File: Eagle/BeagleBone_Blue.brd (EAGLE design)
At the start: 86.4 x 54.6 mm, 297 parts, among them M1 JST_ZH_2, M2 JST_ZH_2, M3 JST_ZH_2, M4 JST_ZH_2, P10 SCHA5B0200, Q3 MOSFET-N, U1 TPD4S012_DRY_6, U4 TPD4S012_DRY_6, U5 24LC_32AT-I/OT, U6 SN74LVC1G07_DCK_5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

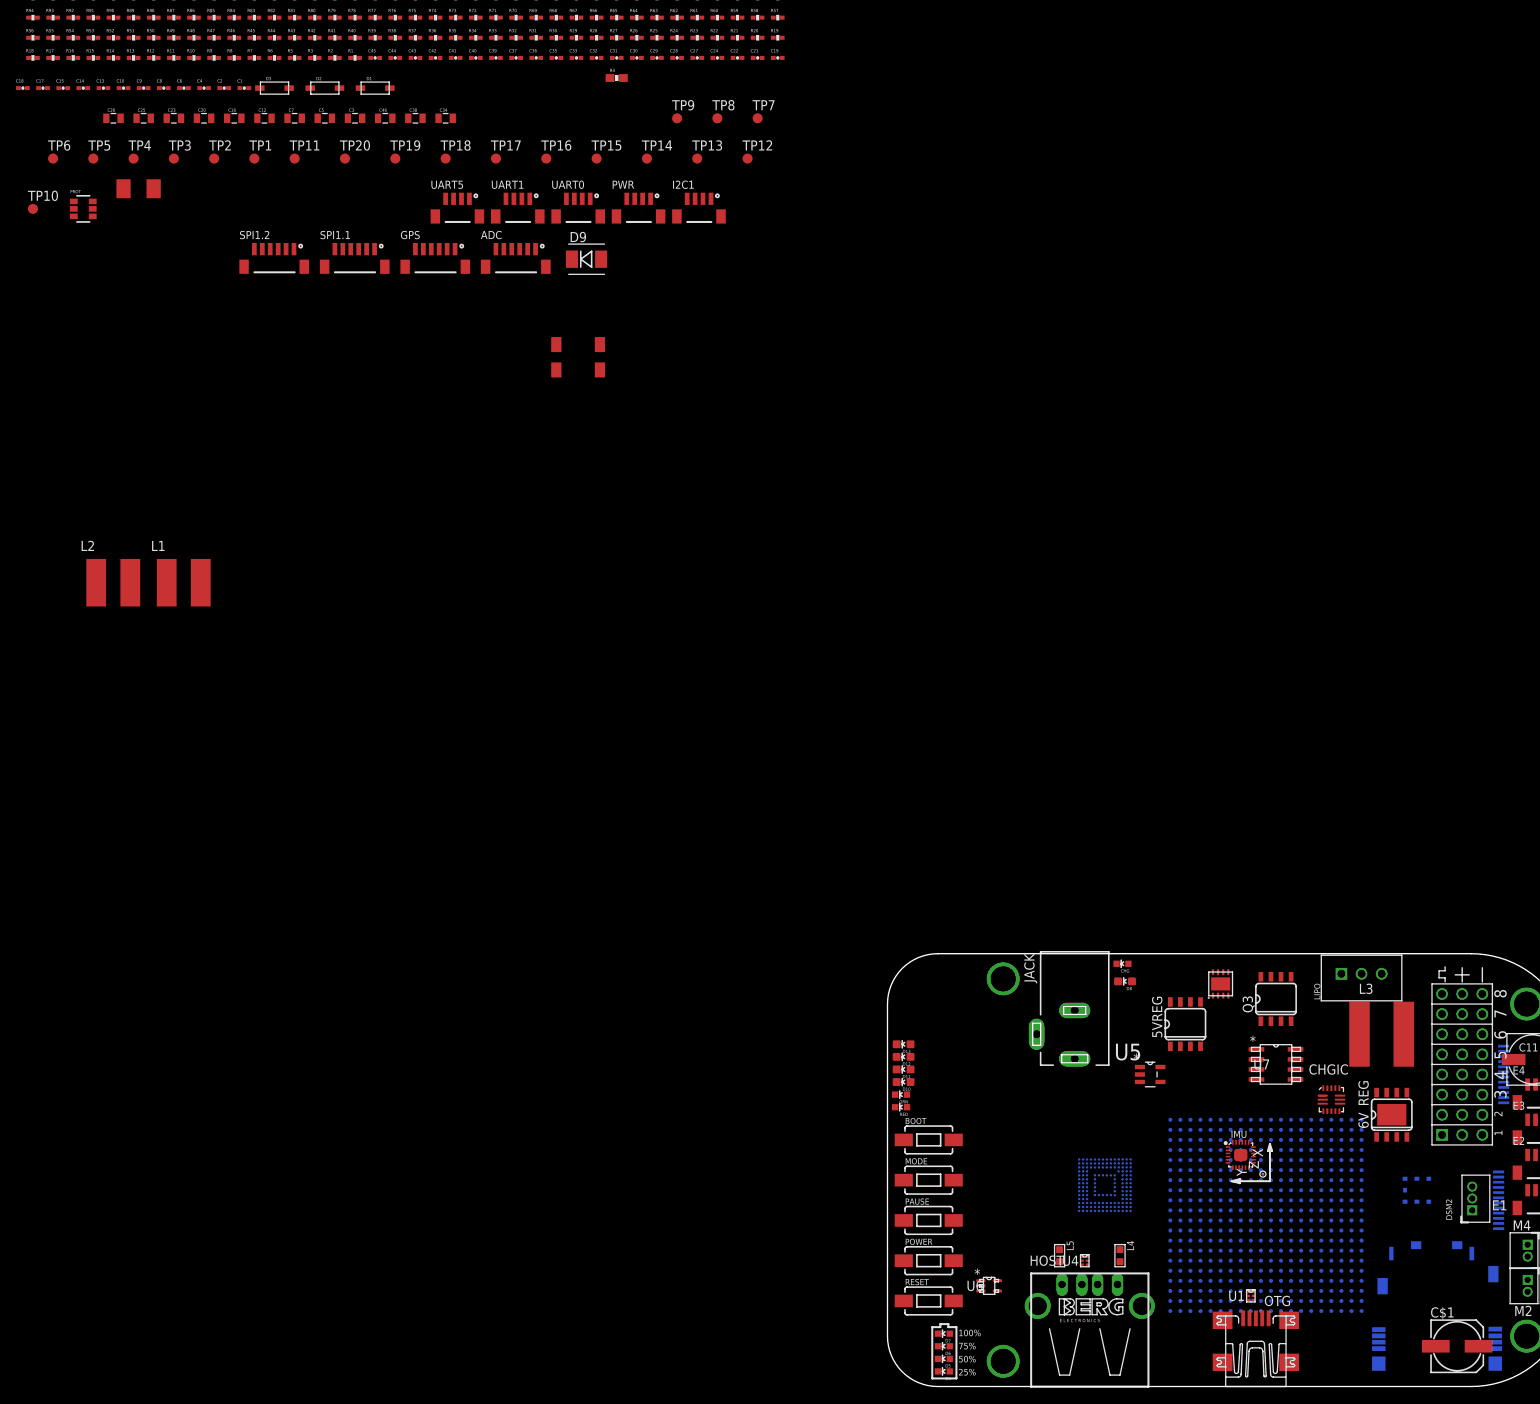
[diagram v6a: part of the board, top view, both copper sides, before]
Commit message: Rough placed a bunch of parts
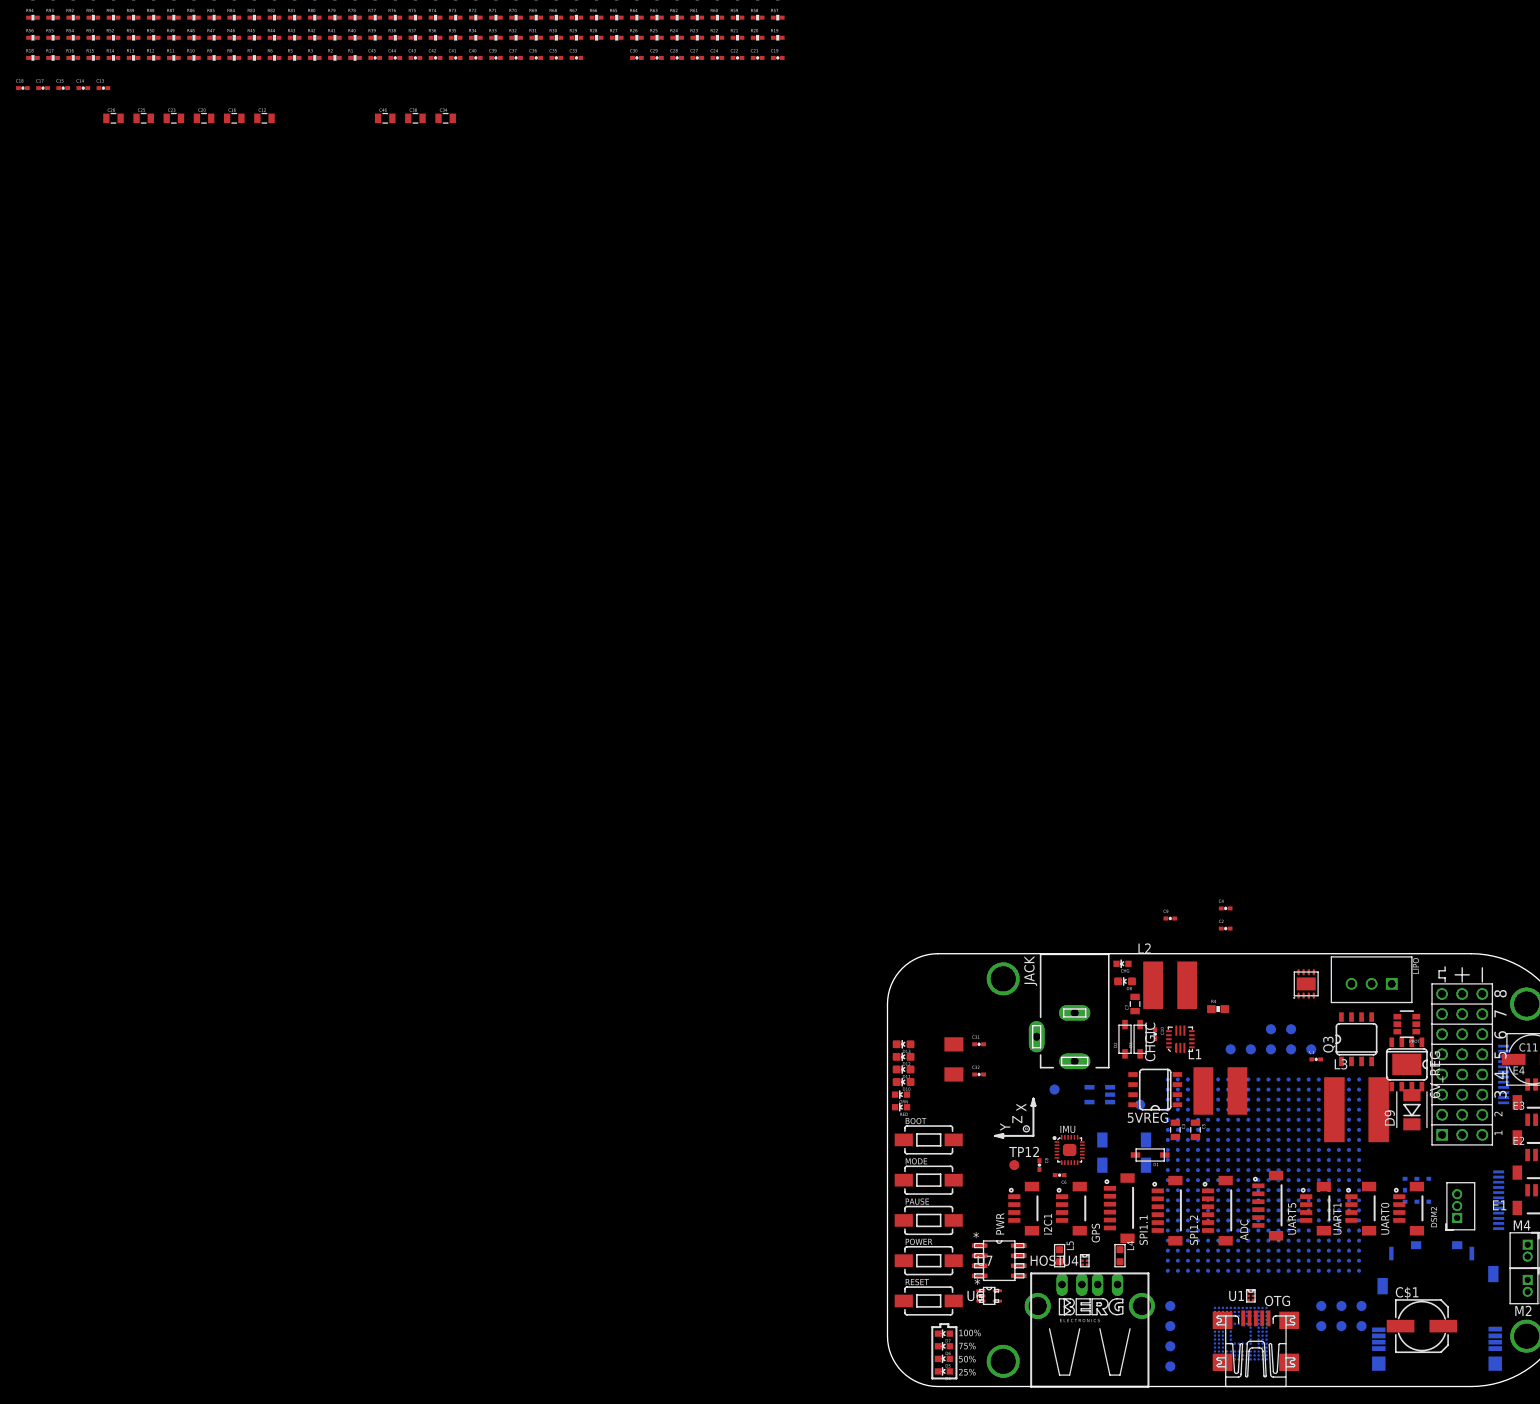
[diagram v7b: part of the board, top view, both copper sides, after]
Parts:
- moved TP6 215.8 mm to (54.6, -44.5), flipped to the bottom
- moved TP4 212.0 mm to (57.1, -47.0), flipped to the bottom
- moved TP3 210.1 mm to (59.7, -47.0), flipped to the bottom
- moved TP2 203.0 mm to (57.1, -44.5), flipped to the bottom
- moved TP10 203.0 mm to (35.6, -49.5), flipped to the bottom
- moved TP1 201.2 mm to (59.7, -44.5), flipped to the bottom
- moved PROT 196.1 mm to (65.4, -8.89), turned to 180 degrees
- moved TP11 188.2 mm to (35.6, -52.1), flipped to the bottom
- moved C1 182.5 mm to (54.0, -13.3)
- moved TP5 178.0 mm to (31.8, -19.1), flipped to the bottom
- moved C10 176.6 mm to (33.7, -10.2), turned to 270 degrees
- moved C6 176.1 mm to (21.6, -27.9), turned to 180 degrees
- moved C8 175.1 mm to (19.1, -26.7), turned to 270 degrees
- moved SPI1.2 172.7 mm to (40.3, -34.9), turned to 90 degrees
- moved C5 168.4 mm to (38.7, -22.2), turned to 270 degrees
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
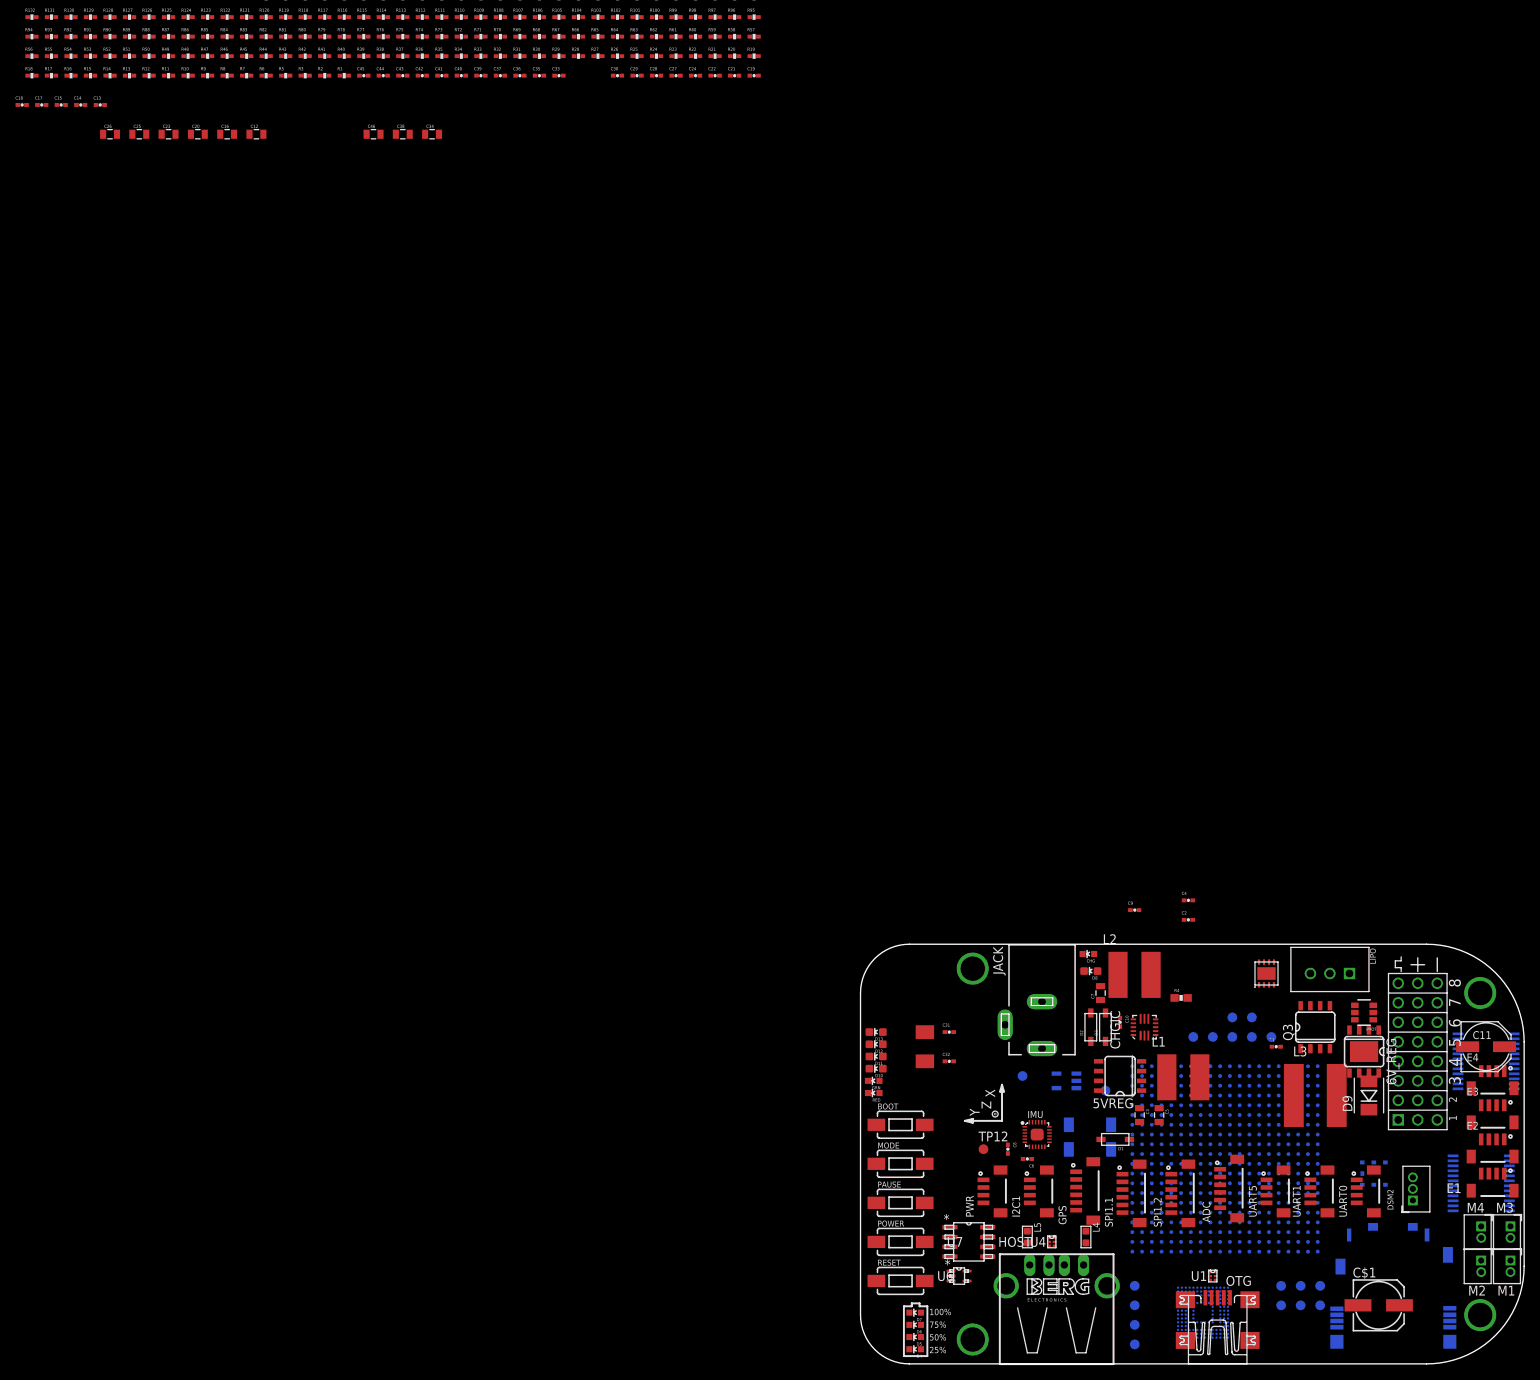
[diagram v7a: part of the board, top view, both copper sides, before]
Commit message: Rough placed a bunch of parts
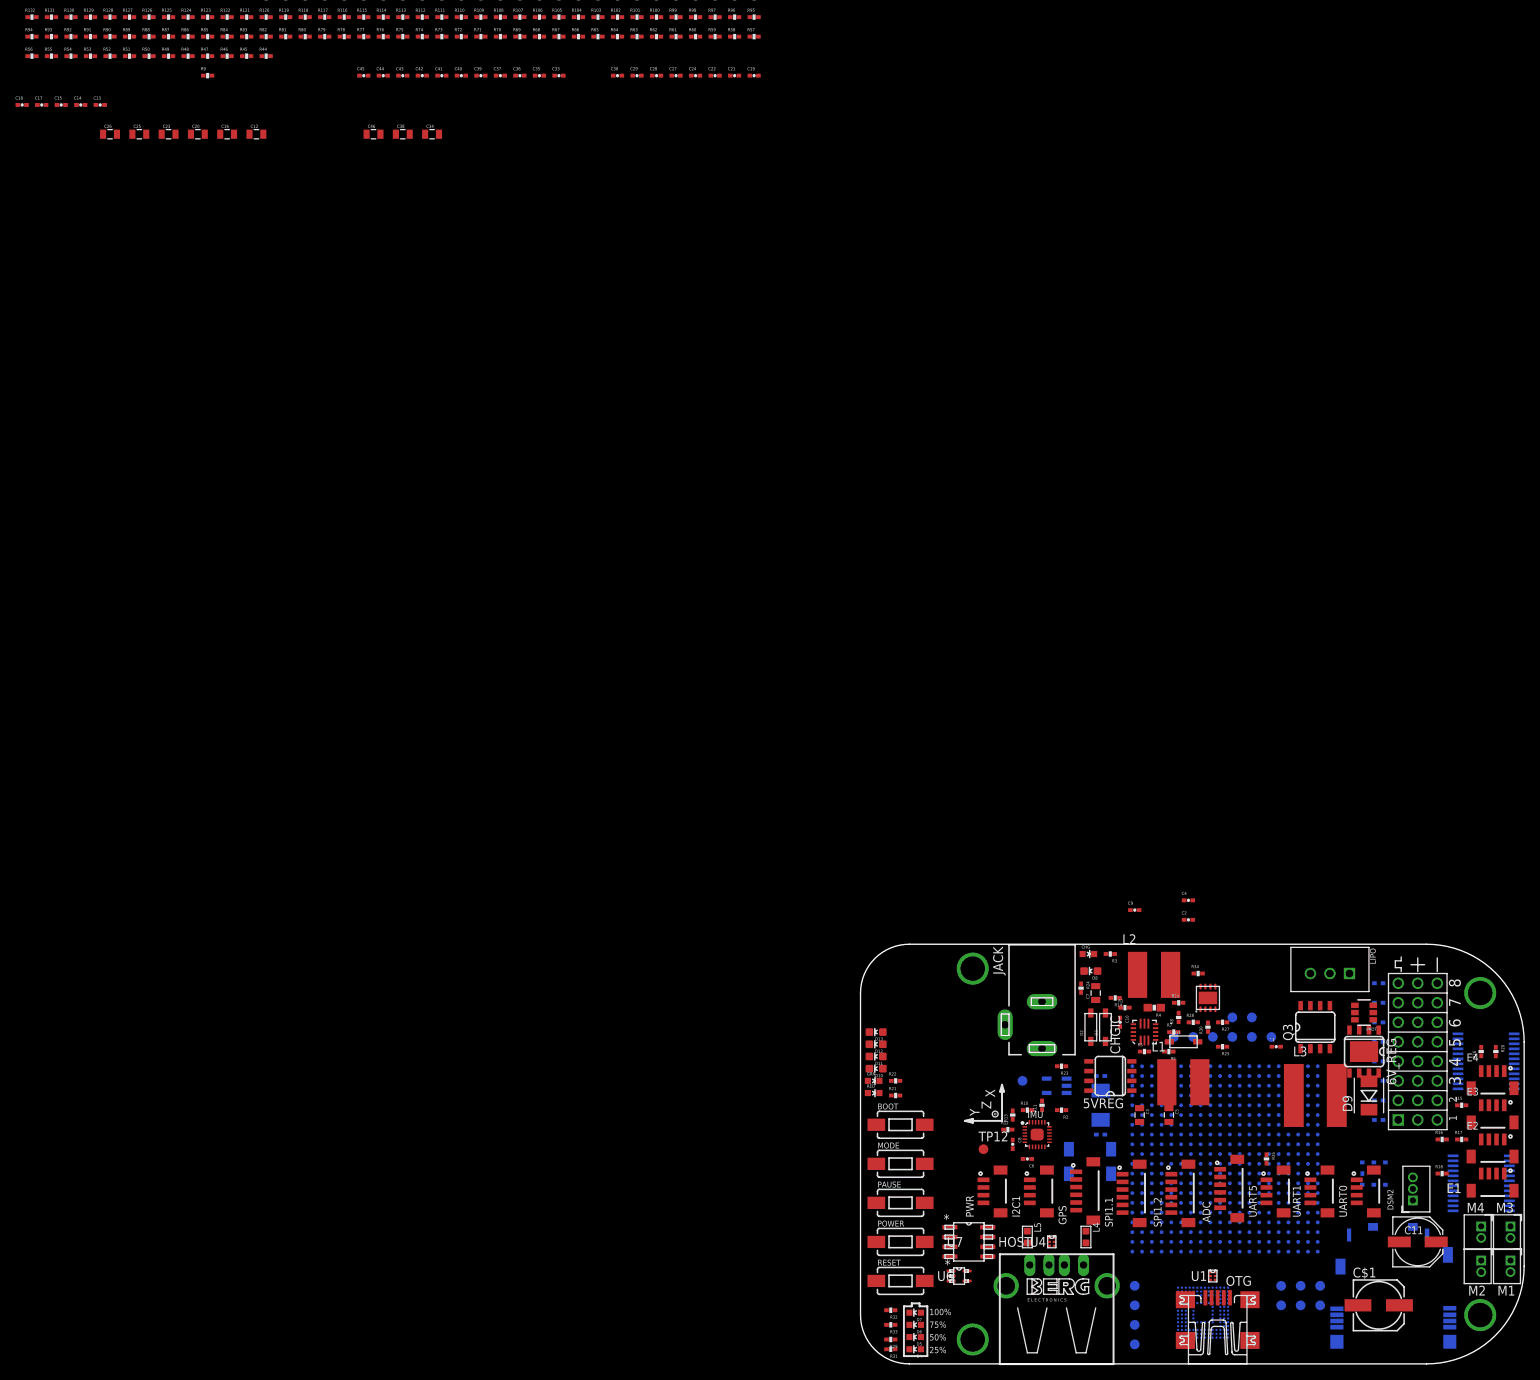
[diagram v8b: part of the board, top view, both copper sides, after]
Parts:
- moved R18 232.6 mm to (75.6, -29.8)
- moved R17 229.9 mm to (78.1, -25.4)
- moved R16 225.8 mm to (75.6, -25.4)
- moved R15 223.1 mm to (78.1, -21.0)
- moved R43 186.5 mm to (67.3, -5.08), flipped to the bottom, turned to 180 degrees
- moved R42 186.3 mm to (67.3, -7.62), flipped to the bottom, turned to 180 degrees
- moved R36 186.2 mm to (67.3, -22.9), flipped to the bottom, turned to 180 degrees
- moved R41 186.1 mm to (67.3, -10.2), flipped to the bottom, turned to 180 degrees
- moved R37 186.0 mm to (67.3, -20.3), flipped to the bottom, turned to 180 degrees
- moved R40 185.9 mm to (67.3, -12.7), flipped to the bottom, turned to 180 degrees
- moved R38 185.9 mm to (67.3, -17.8), flipped to the bottom, turned to 180 degrees
- moved R39 185.9 mm to (67.3, -15.2), flipped to the bottom, turned to 180 degrees
- moved R35 179.2 mm to (52.7, -27.9), turned to 270 degrees
- moved R14 177.5 mm to (33.0, -6.99), turned to 180 degrees
- moved R13 177.5 mm to (19.7, -22.2), turned to 90 degrees
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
